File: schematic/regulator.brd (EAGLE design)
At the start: 63 x 45 mm, 30 parts, among them J2 STOP_LIGHT, J3 ON/OFF, J4 BATTERY, J5 DRIVER, J6 DRIVER POWER, Q1 PMOSFET, Q2 NPN, Q3 PMOSFET, Q4 PMOSFET, Q7 NMOSFET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

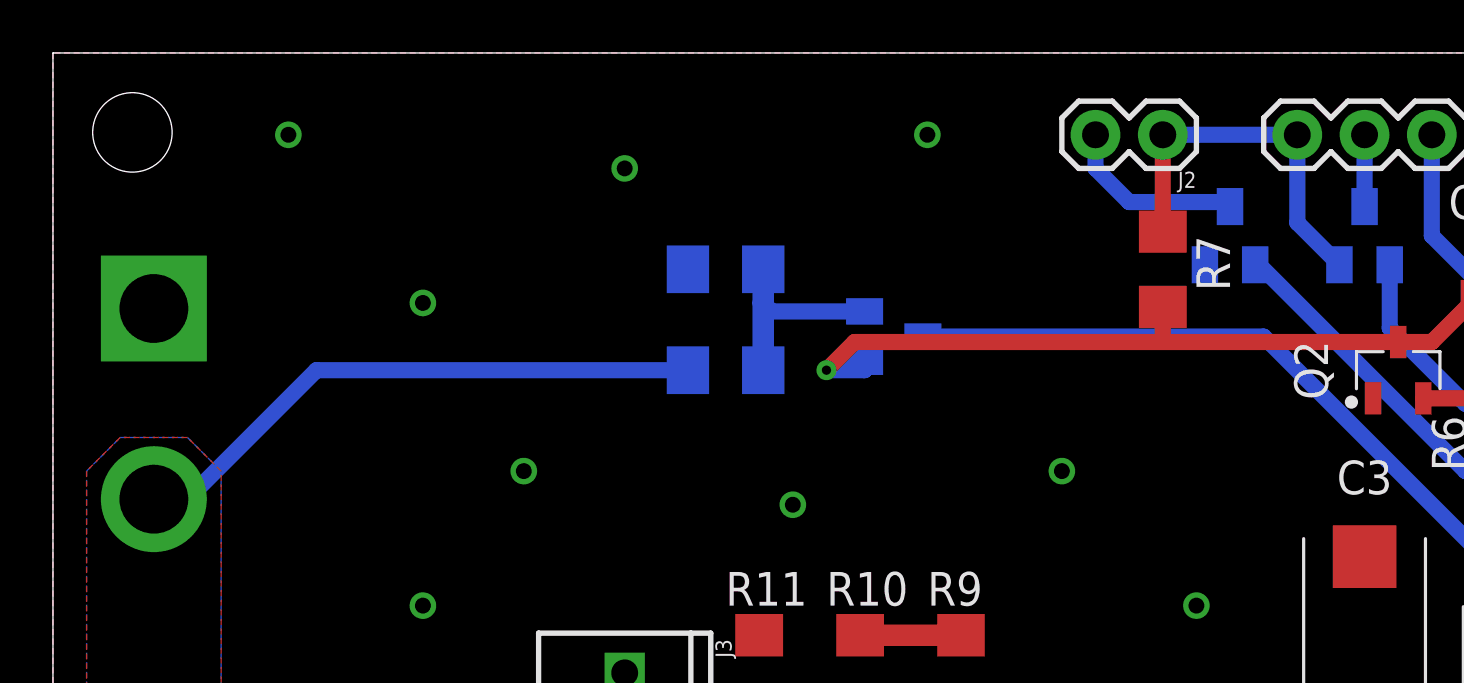
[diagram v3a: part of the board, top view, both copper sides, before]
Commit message: Cosmetical updates on schematics
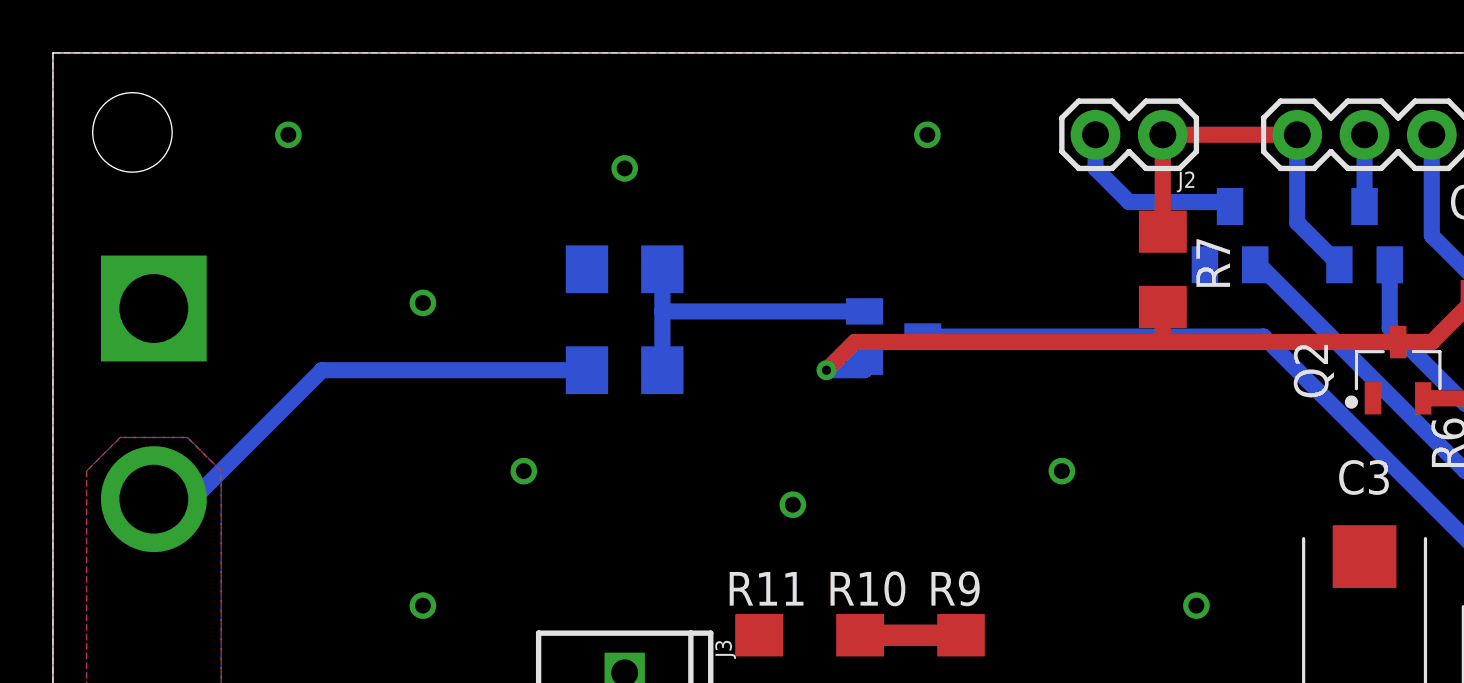
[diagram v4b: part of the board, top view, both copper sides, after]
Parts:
- J7: value (none) -> COMM
- moved R4 3.81 mm to (21.6, 36.8)
- moved R5 3.81 mm to (21.6, 33.0)
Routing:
- net VIN: track 50.4 -> 46.2 mm
- net BATOUT: track 9.04 -> 11.4 mm
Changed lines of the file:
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@@
 <attribute name="VALUE" x="-0.29" y="34.85" size="1.27" layer="27" rot="R270"/>
 </element>
-<element name="J7" library="SparkFun-Connectors" library_urn="urn:adsk.eagle:library:513" package="1X06_LONGPADS" package3d_urn="urn:adsk.eagle:package:37991/1" value="" x="59.69" y="24.13" smashed="yes" rot="R90">
+<element name="J7" library="SparkFun-Connectors" library_urn="urn:adsk.eagle:library:513" package="1X06_LONGPADS" package3d_urn="urn:adsk.eagle:package:37991/1" value="COMM" x="59.69" y="24.13" smashed="yes" rot="R90">
 <attribute name="NAME" x="57.658" y="22.86" size="0.6096" layer="25" font="vector" ratio="20" rot="R90"/>
 <attribute name="VALUE" x="62.357" y="22.86" size="0.6096" layer="27" font="vector" ratio="20" rot="R90"/>
@@
 <attribute name="SPICEMODEL" value="NONE" x="67.31" y="-19.05" size="1.778" layer="28" rot="MR270" display="off"/>
 <attribute name="SPICEPREFIX" value="R" x="67.31" y="-19.05" size="1.778" layer="28" rot="MR270" display="off"/>
-</element>
-<element name="R4" library="eagle-ltspice" library_urn="urn:adsk.eagle:library:217" package="R1206" package3d_urn="urn:adsk.eagle:package:13301/1" value="133K" x="25.4" y="36.83" smashed="yes" rot="MR180">
-<attribute name="NAME" x="26.67" y="38.1" size="1.27" layer="26" rot="MR0"/>
-<attribute name="SPICEMODEL" value="NONE" x="41.91" y="92.71" size="1.778" layer="28" rot="MR180" display="off"/>
-<attribute name="SPICEPREFIX" value="R" x="41.91" y="92.71" size="1.778" layer="28" rot="MR180" display="off"/>
-</element>
-<element name="R5" library="eagle-ltspice" library_urn="urn:adsk.eagle:library:217" package="R1206" package3d_urn="urn:adsk.eagle:package:13301/1" value="1M" x="25.4" y="33.02" smashed="yes" rot="MR0">
-<attribute name="NAME" x="26.67" y="34.29" size="1.27" layer="26" rot="MR0"/>
-<attribute name="SPICEMODEL" value="NONE" x="-6.35" y="-22.86" size="1.778" layer="28" rot="MR0" display="off"/>
-<attribute name="SPICEPREFIX" value="R" x="-6.35" y="-22.86" size="1.778" layer="28" rot="MR0" display="off"/>
 </element>
 <element name="R9" library="eagle-ltspice" library_urn="urn:adsk.eagle:library:217" package="R1206" package3d_urn="urn:adsk.eagle:package:13301/1" value="47K" x="34.29" y="21.59" smashed="yes" rot="R90">
@@
 <attribute name="TYPE" value="P-Channel" x="31.75" y="34.29" size="1.778" layer="28" rot="MR90" display="off"/>
 <attribute name="VALUE" x="28.575" y="32.385" size="1.27" layer="28" rot="MR90"/>
+</element>
+<element name="R4" library="eagle-ltspice" library_urn="urn:adsk.eagle:library:217" package="R1206" package3d_urn="urn:adsk.eagle:package:13301/1" value="133K" x="21.59" y="36.83" smashed="yes" rot="MR180">
+<attribute name="NAME" x="20.32" y="35.56" size="1.27" layer="26" rot="MR180"/>
+<attribute name="SPICEMODEL" value="NONE" x="21.59" y="36.83" size="1.778" layer="28" rot="MR180" display="off"/>
+<attribute name="SPICEPREFIX" value="R" x="21.59" y="36.83" size="1.778" layer="28" rot="MR180" display="off"/>
+<attribute name="VALUE" x="20.32" y="39.37" size="1.27" layer="28" rot="MR180"/>
+</element>
+<element name="R5" library="eagle-ltspice" library_urn="urn:adsk.eagle:library:217" package="R1206" package3d_urn="urn:adsk.eagle:package:13301/1" value="1M" x="21.59" y="33.02" smashed="yes" rot="MR0">
+<attribute name="NAME" x="22.86" y="34.29" size="1.27" layer="26" rot="MR0"/>
+<attribute name="SPICEMODEL" value="NONE" x="21.59" y="33.02" size="1.778" layer="28" rot="MR0" display="off"/>
+<attribute name="SPICEPREFIX" value="R" x="21.59" y="33.02" size="1.778" layer="28" rot="MR0" display="off"/>
+<attribute name="VALUE" x="22.86" y="30.48" size="1.27" layer="28" rot="MR0"/>
 </element>
 </elements>
@@
 <signal name="5V">
 <contactref element="J5" pad="4"/>
-<contactref element="J2" pad="1"/>
 <contactref element="Q3" pad="2"/>
 <contactref element="R7" pad="1"/>
 <wire x1="48.58" y1="37" x2="46.99" y2="38.59" width="0.6096" layer="16"/>
 <wire x1="46.99" y1="38.59" x2="46.99" y2="41.91" width="0.6096" layer="16"/>
-<wire x1="41.91" y1="41.91" x2="46.99" y2="41.91" width="0.6096" layer="16"/>
-<wire x1="41.91" y1="38.252" x2="41.91" y2="41.91" width="0.6096" layer="1"/>
+<contactref element="J2" pad="1"/>
+<wire x1="41.91" y1="41.91" x2="41.91" y2="38.252" width="0.6096" layer="1"/>
+<wire x1="41.91" y1="41.91" x2="46.99" y2="41.91" width="0.6096" layer="1"/>
 </signal>
 <signal name="STLEDOUT">
@@
 <contactref element="J6" pad="VCC"/>
 <contactref element="R5" pad="2"/>
-<wire x1="4.445" y1="27.515" x2="9.95" y2="33.02" width="0.6096" layer="16"/>
-<wire x1="9.95" y1="33.02" x2="23.978" y2="33.02" width="0.6096" layer="16"/>
-<wire x1="3.81" y1="28.15" x2="4.445" y2="27.515" width="0.6096" layer="16"/>
+<wire x1="10.16" y1="33.02" x2="5.08" y2="27.94" width="0.6096" layer="16"/>
+<wire x1="5.08" y1="27.94" x2="4.02" y2="27.94" width="0.6096" layer="16"/>
+<wire x1="4.02" y1="27.94" x2="3.81" y2="28.15" width="0.6096" layer="16"/>
+<wire x1="20.168" y1="33.02" x2="10.16" y2="33.02" width="0.6096" layer="16"/>
 </signal>
 <signal name="GND">
@@
 <contactref element="J4" pad="GND"/>
 <contactref element="R11" pad="2"/>
-<contactref element="R4" pad="1"/>
 <polygon width="0.8128" layer="1" rank="6">
 <vertex x="0" y="45"/>
@@
 <via x="21.59" y="3.81" extent="1-16" drill="0.6"/>
 <via x="27.94" y="16.51" extent="1-16" drill="0.6"/>
+<contactref element="R4" pad="1"/>
 </signal>
 <signal name="BATOUT">
+<contactref element="Q4" pad="2"/>
 <contactref element="R4" pad="2"/>
 <contactref element="R5" pad="1"/>
-<wire x1="26.822" y1="36.83" x2="26.822" y2="35.56" width="0.8128" layer="16"/>
-<contactref element="Q4" pad="2"/>
-<wire x1="26.822" y1="35.56" x2="26.822" y2="33.02" width="0.8128" layer="16"/>
-<wire x1="26.822" y1="33.02" x2="26.822" y2="34.29" width="0.6096" layer="16"/>
-<wire x1="30.65" y1="35.24" x2="27.142" y2="35.24" width="0.6096" layer="16"/>
-<wire x1="27.142" y1="35.24" x2="26.822" y2="35.56" width="0.6096" layer="16"/>
+<wire x1="23.012" y1="36.83" x2="23.012" y2="35.24" width="0.6096" layer="16"/>
+<wire x1="23.012" y1="35.24" x2="23.012" y2="33.02" width="0.6096" layer="16"/>
+<wire x1="23.012" y1="35.24" x2="30.65" y2="35.24" width="0.6096" layer="16"/>
 </signal>
 <signal name="SPEED_DR">
